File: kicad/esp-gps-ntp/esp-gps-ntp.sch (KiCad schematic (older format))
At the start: 26 parts, among them J1 Power, J2 Serial, J3 JTAG, J4 Display, J5 GPS, J6 UltimateGPS, SW1 Reset, U1 MCP1825-3302E, U2 ESP32-WROOM-32D, U3 DS3231M

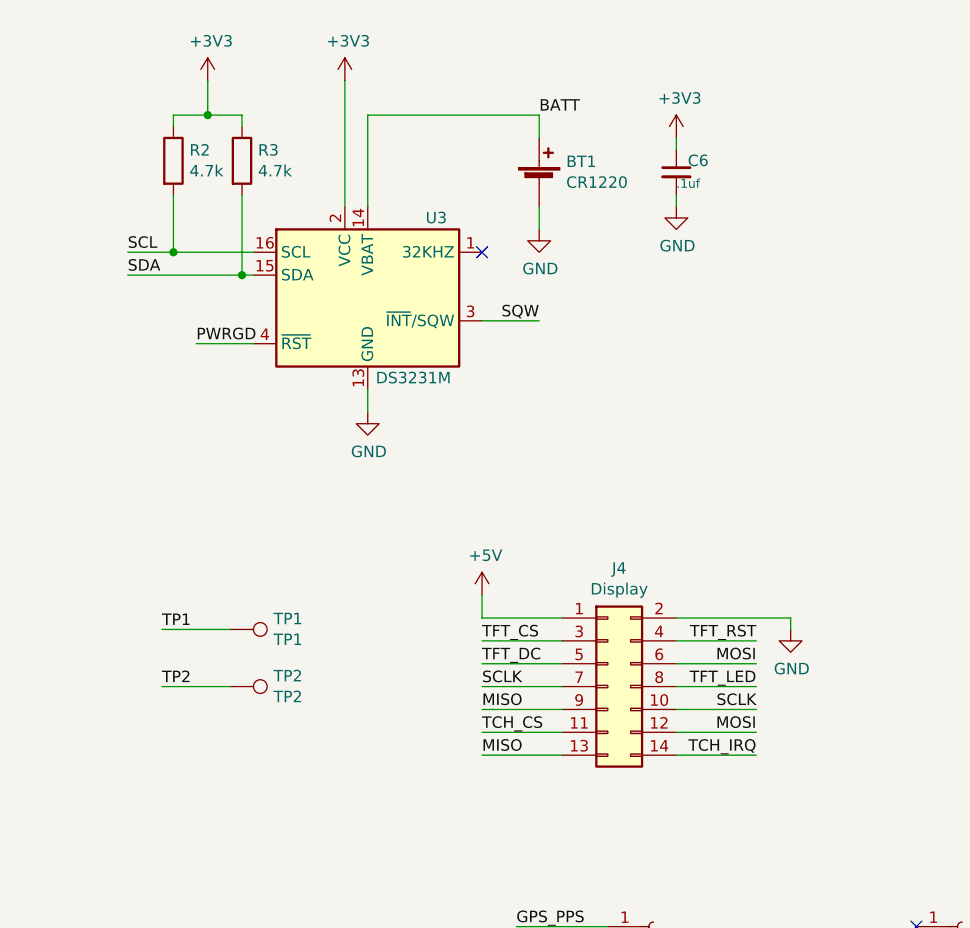
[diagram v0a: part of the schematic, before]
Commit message: new board version fix idle time hack
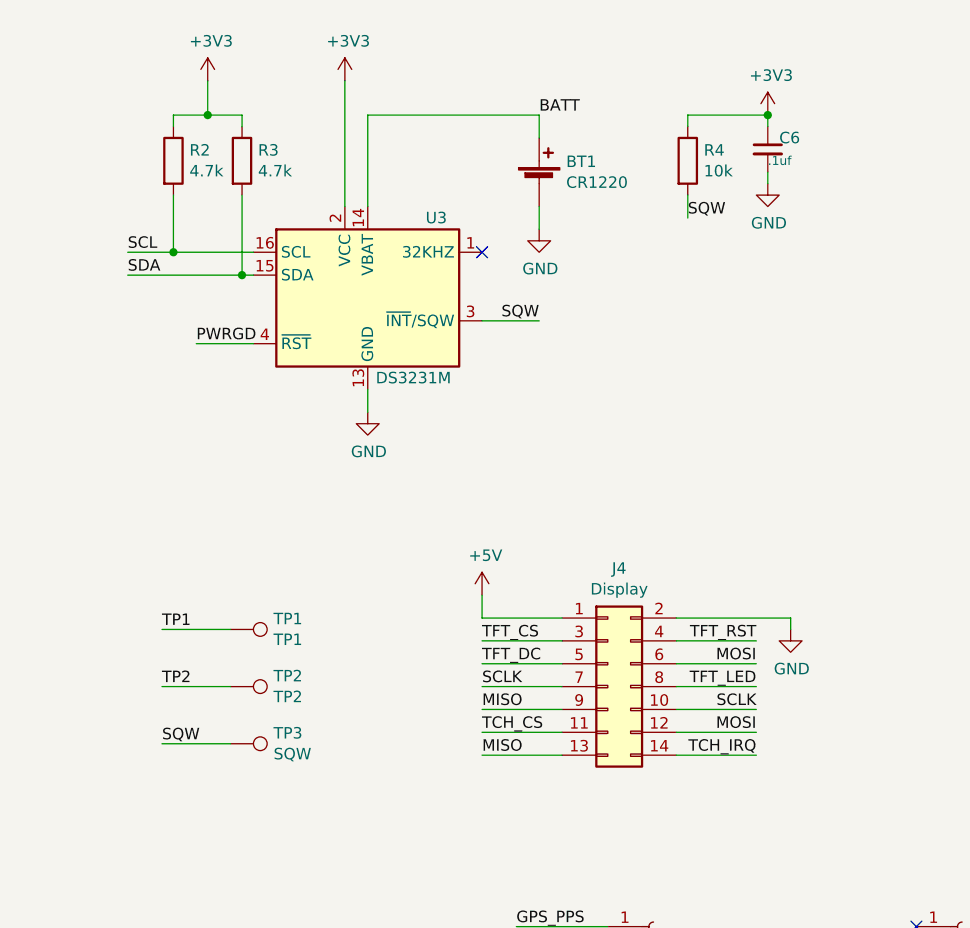
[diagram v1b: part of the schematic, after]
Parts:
- added R4: 10k, Resistor_THT:R_Axial_DIN0207_L6.3mm_D2.5mm_P7.62mm_Horizontal, symbol Device:R
- added TP3: SQW, TestPoint:TestPoint_THTPad_2.5x2.5mm_Drill1.2mm, symbol Connector:TestPoint
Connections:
- net +3V3: now also R4.1
- net SQW: now also R4.2, TP3.1
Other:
- moved on the sheet: C6
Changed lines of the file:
@@
-$EndComp
-$Comp
-L Device:C_Small C6
-U 1 1 5FC77703
-P 7400 1550
-F 0 "C6" H 7450 1600 50  0000 L CNN
-F 1 ".1uf" H 7400 1500 39  0000 L CNN
-F 2 "Capacitor_THT:C_Disc_D5.0mm_W2.5mm_P2.50mm" H 7400 1550 50  0001 C CNN
-F 3 "~" H 7400 1550 50  0001 C CNN
-	1    7400 1550
-	1    0    0    -1
-$EndComp
-$Comp
-L power:GND #PWR016
-U 1 1 5FC7A201
-P 7400 1700
-F 0 "#PWR016" H 7400 1450 50  0001 C CNN
-F 1 "GND" H 7405 1527 50  0000 C CNN
-F 2 "" H 7400 1700 50  0001 C CNN
-F 3 "" H 7400 1700 50  0001 C CNN
-	1    7400 1700
-	1    0    0    -1
 $EndComp
 $Comp
@@
 	1    0    0    -1
 $EndComp
-$Comp
-L power:+3V3 #PWR015
-U 1 1 5FCF7B68
-P 7400 1400
-F 0 "#PWR015" H 7400 1250 50  0001 C CNN
-F 1 "+3V3" H 7415 1573 50  0000 C CNN
-F 2 "" H 7400 1400 50  0001 C CNN
-F 3 "" H 7400 1400 50  0001 C CNN
-	1    7400 1400
-	1    0    0    -1
-$EndComp
-Wire Wire Line
-	7400 1400 7400 1450
-Wire Wire Line
-	7400 1650 7400 1700
 Wire Wire Line
 	5950 1700 5950 1150
@@
 TP2
 NoConn ~ 1350 6750
-$Comp
-L Device:Battery_Cell BT1
-U 1 1 5FDA92C1
-P 6800 1600
-F 0 "BT1" H 6918 1696 50  0000 L CNN
-F 1 "CR1220" H 6918 1605 50  0000 L CNN
-F 2 "HARWIN-CR1220:HARWIN-CR1220" V 6800 1660 50  0001 C CNN
-F 3 "~" V 6800 1660 50  0001 C CNN
-	1    6800 1600
-	1    0    0    -1
-$EndComp
-$Comp
-L power:GND #PWR0101
-U 1 1 5FDC2157
-P 6800 1800
-F 0 "#PWR0101" H 6800 1550 50  0001 C CNN
-F 1 "GND" H 6805 1627 50  0000 C CNN
-F 2 "" H 6800 1800 50  0001 C CNN
-F 3 "" H 6800 1800 50  0001 C CNN
-	1    6800 1800
-	1    0    0    -1
-$EndComp
-Wire Wire Line
-	6800 1400 6800 1300
-Wire Wire Line
-	6800 1300 6050 1300
 Wire Wire Line
 	6050 1300 6050 1700
-Wire Wire Line
-	6800 1700 6800 1800
 $Comp
 L Mechanical:MountingHole H1
@@
 	1    0    0    -1
 $EndComp
-Text Label 6800 1300 0    50   ~ 0
-BATT
 NoConn ~ 8450 4850
 NoConn ~ 8450 4950
@@
 Text Label 4300 4250 2    50   ~ 0
 TCH_IRQ
+$Comp
+L Connector:TestPoint TP3
+U 1 1 5FD8561E
+P 5450 4050
+F 0 "TP3" V 5404 4238 50  0000 L CNN
+F 1 "SQW" V 5495 4238 50  0000 L CNN
+F 2 "TestPoint:TestPoint_THTPad_2.5x2.5mm_Drill1.2mm" H 5650 4050 50  0001 C CNN
+F 3 "~" H 5650 4050 50  0001 C CNN
+	1    5450 4050
+	0    1    1    0
+$EndComp
+Wire Wire Line
+	5450 4050 5150 4050
+Text Label 5150 4050 0    50   ~ 0
+SQW
+$Comp
+L Device:R R4
+U 1 1 5FD8CDD5
+P 7450 1500
+F 0 "R4" H 7520 1546 50  0000 L CNN
+F 1 "10k" H 7520 1455 50  0000 L CNN
+F 2 "Resistor_THT:R_Axial_DIN0207_L6.3mm_D2.5mm_P7.62mm_Horizontal" V 7380 1500 50  0001 C CNN
+F 3 "~" H 7450 1500 50  0001 C CNN
+	1    7450 1500
+	1    0    0    -1
+$EndComp
+Text Label 6800 1300 0    50   ~ 0
+BATT
+Wire Wire Line
+	6800 1700 6800 1800
+Wire Wire Line
+	6800 1300 6050 1300
+Wire Wire Line
+	6800 1400 6800 1300
+$Comp
+L power:GND #PWR0101
+U 1 1 5FDC2157
+P 6800 1800
+F 0 "#PWR0101" H 6800 1550 50  0001 C CNN
+F 1 "GND" H 6805 1627 50  0000 C CNN
+F 2 "" H 6800 1800 50  0001 C CNN
+F 3 "" H 6800 1800 50  0001 C CNN
+	1    6800 1800
+	1    0    0    -1
+$EndComp
+$Comp
+L Device:Battery_Cell BT1
+U 1 1 5FDA92C1
+P 6800 1600
+F 0 "BT1" H 6918 1696 50  0000 L CNN
+F 1 "CR1220" H 6918 1605 50  0000 L CNN
+F 2 "HARWIN-CR1220:HARWIN-CR1220" V 6800 1660 50  0001 C CNN
+F 3 "~" V 6800 1660 50  0001 C CNN
+	1    6800 1600
+	1    0    0    -1
+$EndComp
+Wire Wire Line
+	7800 1550 7800 1600
+Wire Wire Line
+	7800 1300 7800 1350
+$Comp
+L power:+3V3 #PWR015
+U 1 1 5FCF7B68
+P 7800 1300
+F 0 "#PWR015" H 7800 1150 50  0001 C CNN
+F 1 "+3V3" H 7815 1473 50  0000 C CNN
+F 2 "" H 7800 1300 50  0001 C CNN
+F 3 "" H 7800 1300 50  0001 C CNN
+	1    7800 1300
+	1    0    0    -1
+$EndComp
+$Comp
+L power:GND #PWR016
+U 1 1 5FC7A201
+P 7800 1600
+F 0 "#PWR016" H 7800 1350 50  0001 C CNN
+F 1 "GND" H 7805 1427 50  0000 C CNN
+F 2 "" H 7800 1600 50  0001 C CNN
+F 3 "" H 7800 1600 50  0001 C CNN
+	1    7800 1600
+	1    0    0    -1
+$EndComp
+$Comp
+L Device:C_Small C6
+U 1 1 5FC77703
+P 7800 1450
+F 0 "C6" H 7850 1500 50  0000 L CNN
+F 1 ".1uf" H 7800 1400 39  0000 L CNN
+F 2 "Capacitor_THT:C_Disc_D5.0mm_W2.5mm_P2.50mm" H 7800 1450 50  0001 C CNN
+F 3 "~" H 7800 1450 50  0001 C CNN
+	1    7800 1450
+	1    0    0    -1
+$EndComp
+Wire Wire Line
+	7450 1350 7450 1300
+Wire Wire Line
+	7450 1300 7800 1300
+Connection ~ 7800 1300
+Wire Wire Line
+	7450 1650 7450 1750
+Text Label 7450 1750 0    50   ~ 0
+SQW
 $EndSCHEMATC
